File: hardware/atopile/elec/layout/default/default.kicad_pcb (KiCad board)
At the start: 2 copper layers, 48 parts

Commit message: feat(pcb): component placement + board outline 130×90mm
- Placed all 48 components via pcbnew scripting (place_components.py)
- Added Edge.Cuts rectangular outline 130×90 mm
- Fixed atopile_address lookup (short form without VectraAutoLights. prefix)
- Groups: connectors top, fuses, LM7805, optocouplers, ESP32,
  xenon MOSFET driver, gabari relay, fog relay, illum channel

Co-Authored-By: Claude Sonnet 4.6 <noreply@anthropic.com>
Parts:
- moved D8 442.2 mm to (35.0, 79.0), turned to 90 degrees
- moved D7 440.2 mm to (26.9, 79.0), turned to 90 degrees
- moved Q3 439.2 mm to (17.9, 79.0)
- moved R3 437.2 mm to (9.95, 79.0), turned to 90 degrees
- moved D4 329.9 mm to (26.9, 67.0), turned to 90 degrees
- moved D1 327.0 mm to (90.0, 67.0), turned to 90 degrees
- moved Q2 319.2 mm to (17.9, 67.0)
- moved D2 319.0 mm to (120.0, 75.0), turned to 90 degrees
- moved R2 317.2 mm to (9.95, 67.0), turned to 90 degrees
- moved Q1 316.2 mm to (81.0, 67.0)
- moved R1 314.3 mm to (73.0, 67.0), turned to 90 degrees
- moved D5 312.3 mm to (65.0, 67.0), turned to 90 degrees
- moved D6 310.4 mm to (57.0, 67.0), turned to 90 degrees
- moved K2 310.4 mm to (37.0, 67.0)
- moved D3 307.4 mm to (120.0, 67.0), turned to 90 degrees
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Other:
- board outline added: 130 x 90 mm

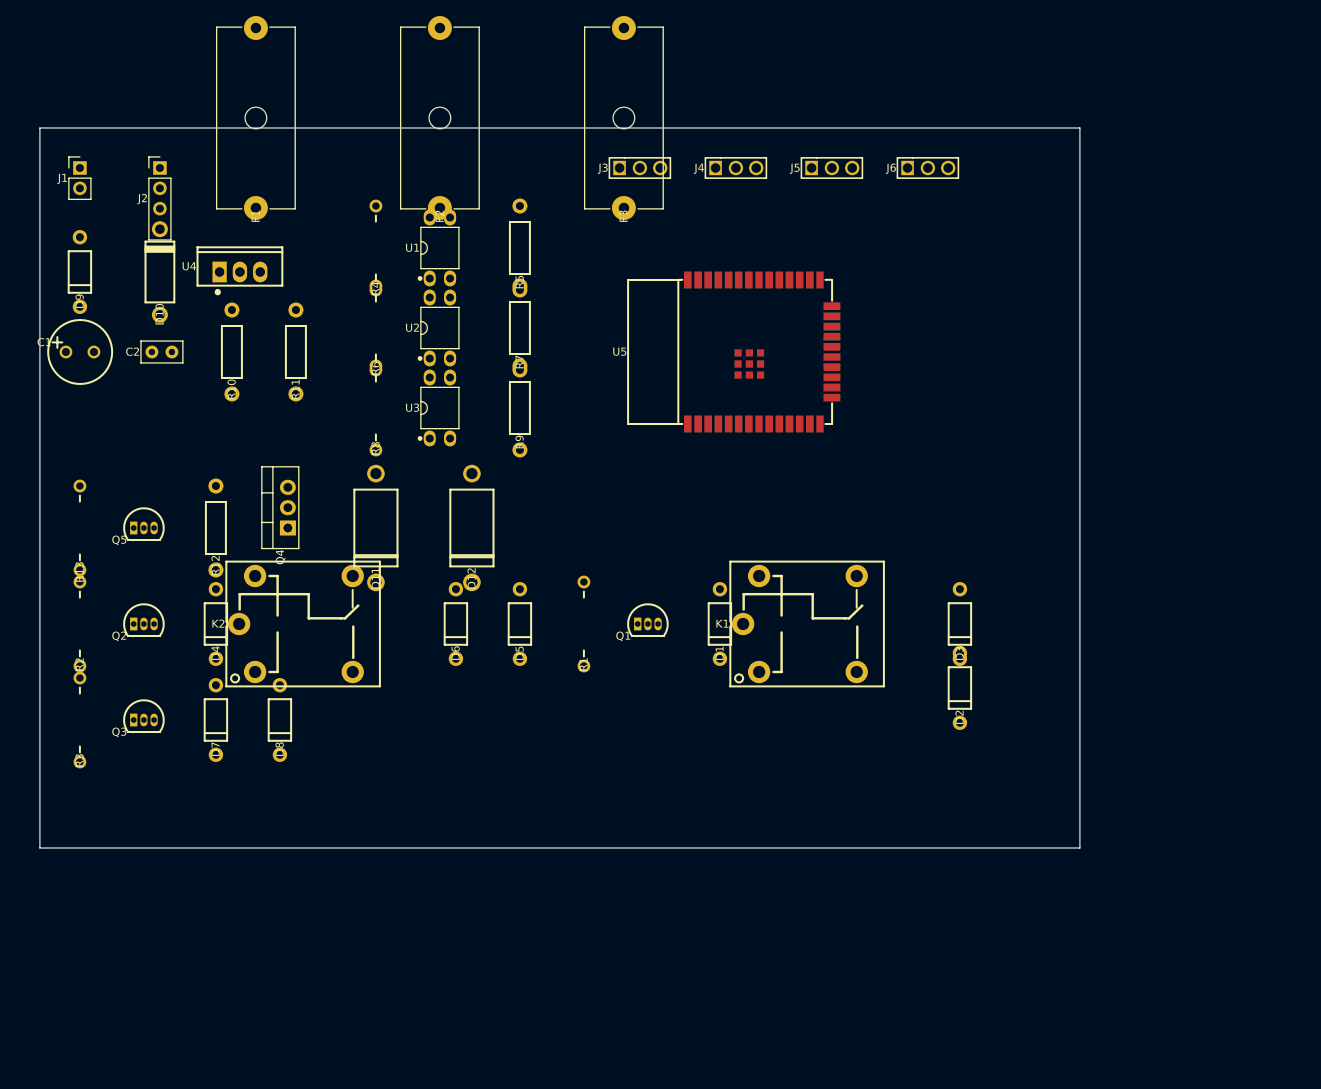
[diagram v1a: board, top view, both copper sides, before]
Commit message: feat(pcb): FreeRouting partial autoroute + improved component spacing
- Increased component spacing (160x120mm board) to eliminate courtyard overlaps
- Added place3.py with generous THT spacing (12-15mm between components)
- FreeRouting autoroute: 35 connections not found (down from 47)
- Exported DSN/SES for FreeRouting workflow
- Remaining: fix D2/D3 short, route 35 ESP32 GPIO connections

Co-Authored-By: Claude Sonnet 4.6 <noreply@anthropic.com>
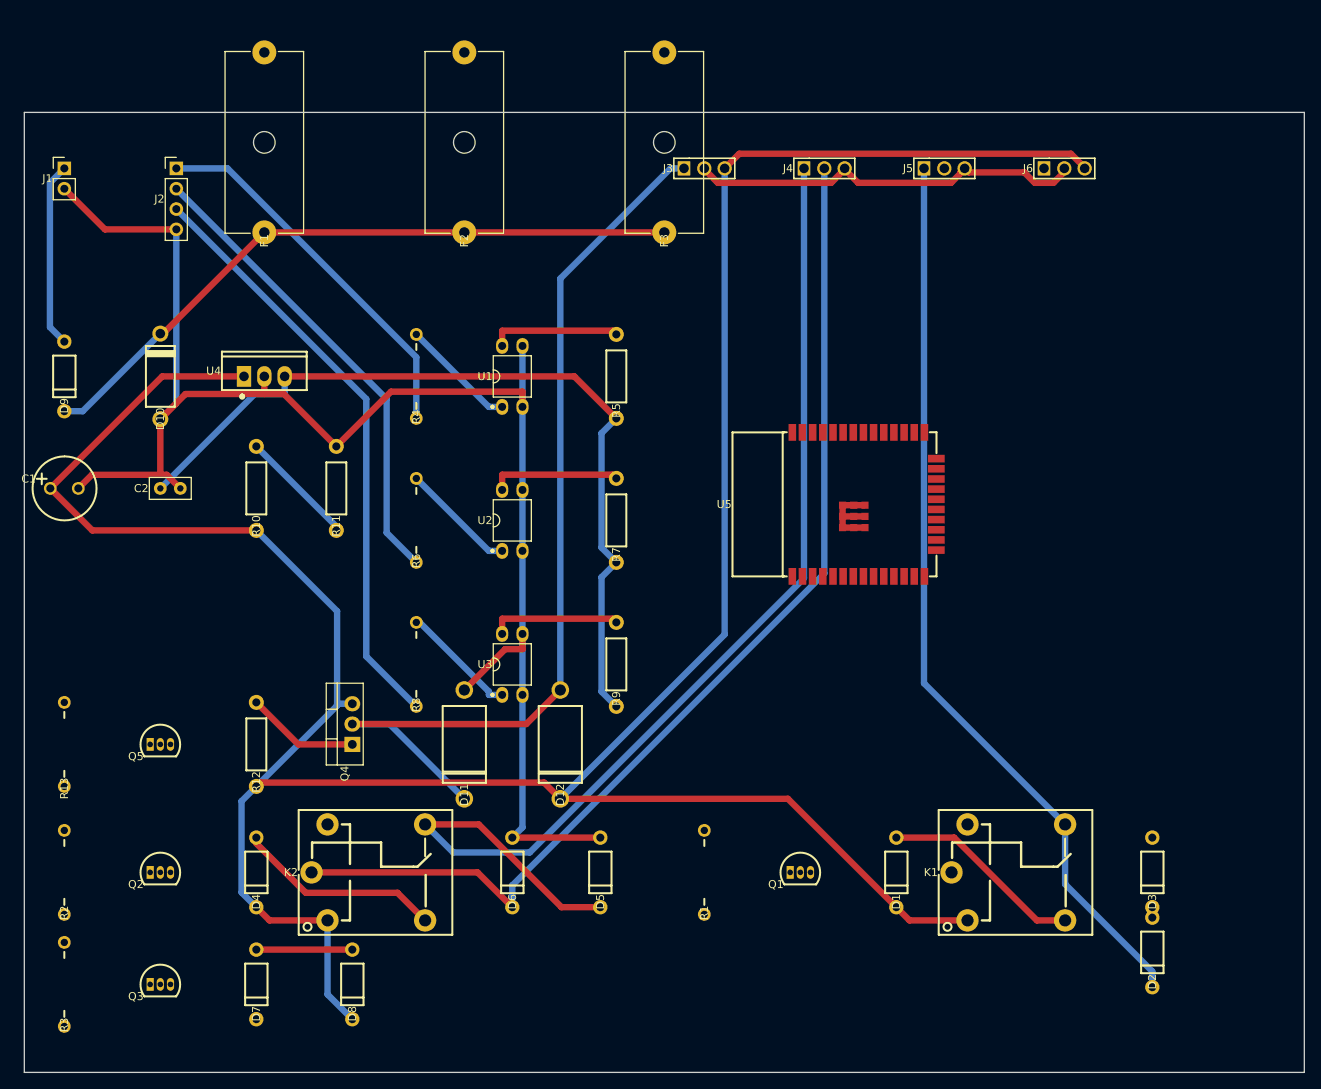
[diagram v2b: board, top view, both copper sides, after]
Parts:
- moved D2 40.9 mm to (144.0, 108.0)
- moved K1 40.5 mm to (126.0, 98.0)
- moved D3 39.3 mm to (144.0, 98.0)
- moved D1 38.1 mm to (112.0, 98.0)
- moved Q1 36.4 mm to (100.0, 98.0)
- moved R1 34.5 mm to (88.0, 98.0)
- moved D8 34.3 mm to (44.0, 112.0)
- moved R9 34.2 mm to (77.0, 72.0)
- moved D7 33.4 mm to (32.0, 112.0)
- moved U3 33.3 mm to (64.0, 72.0)
- moved Q3 33.1 mm to (20.0, 112.0)
- moved R3 33.1 mm to (8.00, 112.0)
- moved D5 32.6 mm to (75.0, 98.0)
- moved R8 32.4 mm to (52.0, 72.0)
- moved K2 32.3 mm to (46.0, 98.0)
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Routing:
- net v12: track 0.00 -> 370.2 mm
- net gnd: track 0.00 -> 275.4 mm
- net com-1: track 0.00 -> 140.4 mm
- net no-1: track 0.00 -> 135.4 mm
- net out_xenon: track 0.00 -> 118.2 mm
- net com: track 0.00 -> 114.2 mm
- net v33: track 0.00 -> 105.3 mm
- net 1: track 0.00 -> 84.3 mm
- net sig_unlock: track 0.00 -> 74.6 mm
- net sig_auto: track 0.00 -> 59.1 mm
- net sig_in: track 0.00 -> 47.4 mm
- net gabari-2: track 0.00 -> 25.8 mm
- net 2: track 0.00 -> 25.4 mm
- net vin_raw: track 0.00 -> 23.1 mm
- net sig_out: track 0.00 -> 16.4 mm
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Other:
- board size 130 x 90 mm -> 160 x 120 mm
